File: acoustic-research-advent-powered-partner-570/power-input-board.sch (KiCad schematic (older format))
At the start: 13 parts, among them J24 DNP, SW1 MAIN POWER

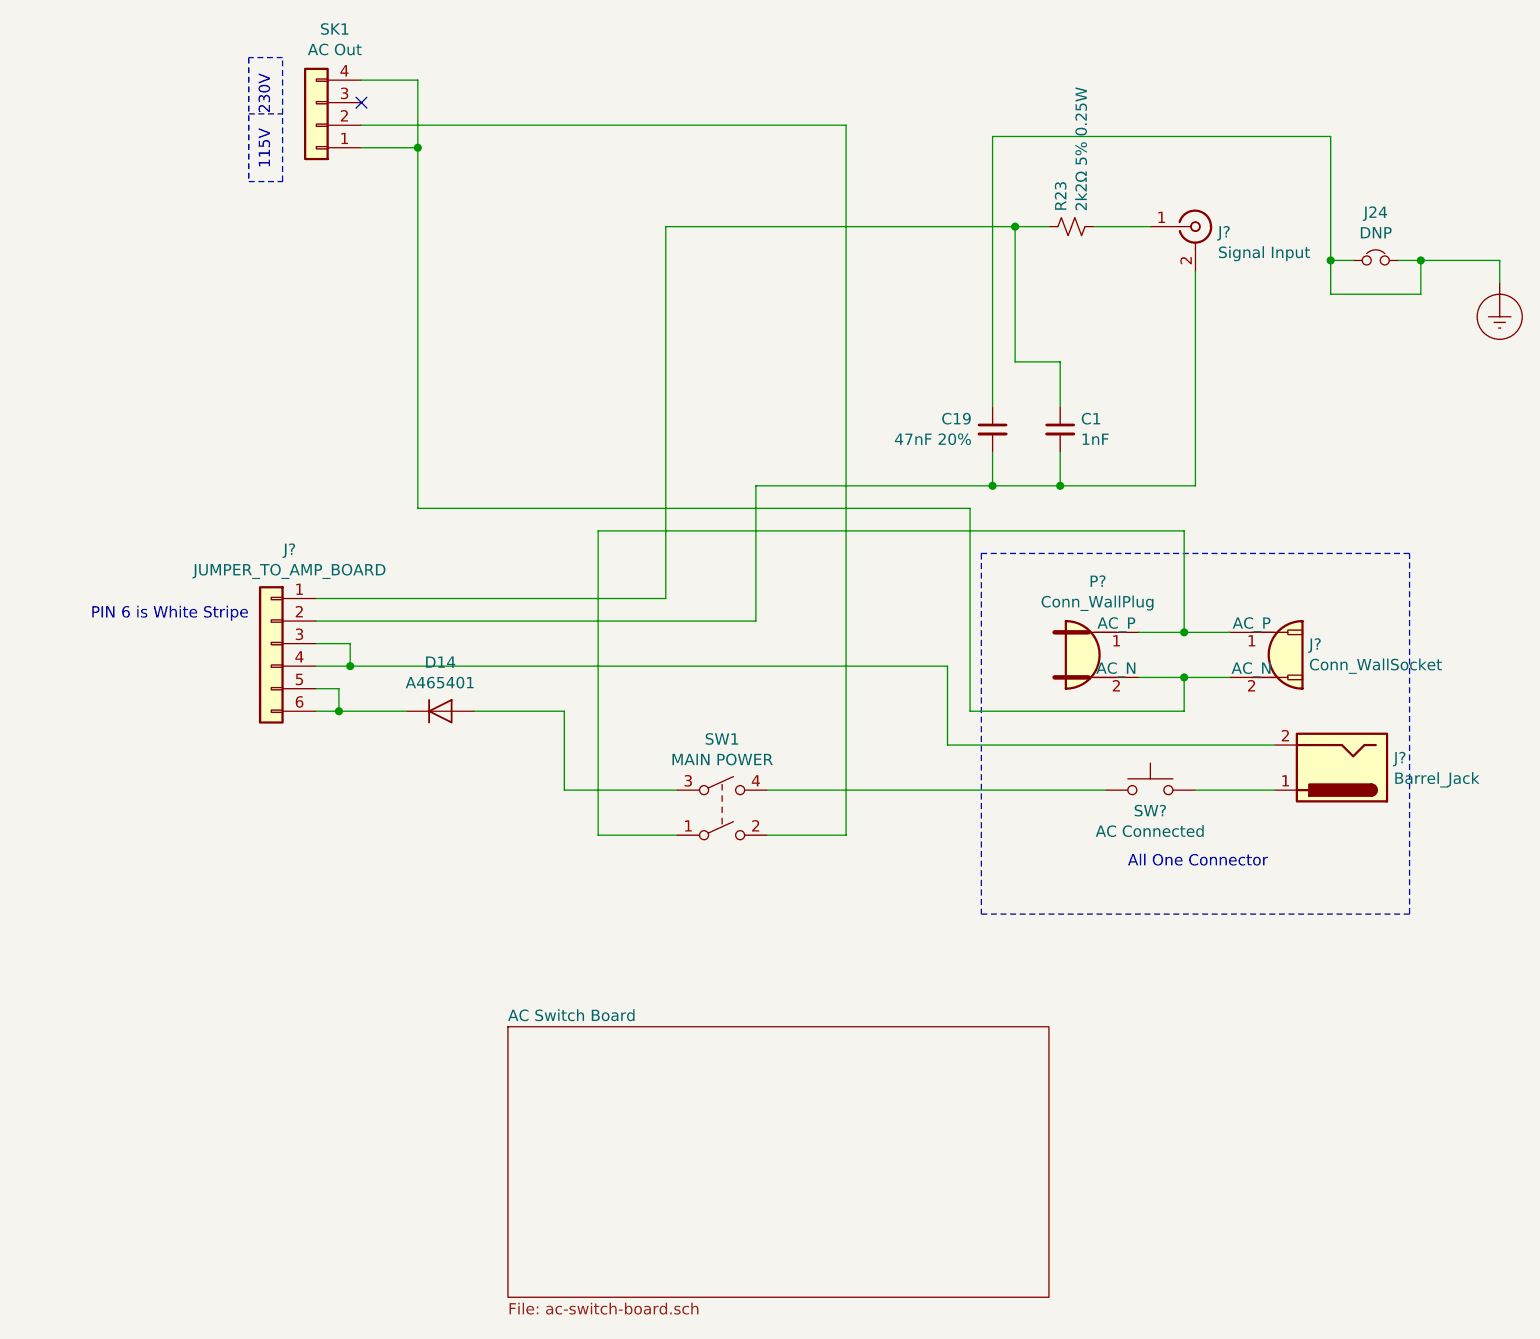
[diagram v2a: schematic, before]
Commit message: trying to clean schematic up a bit
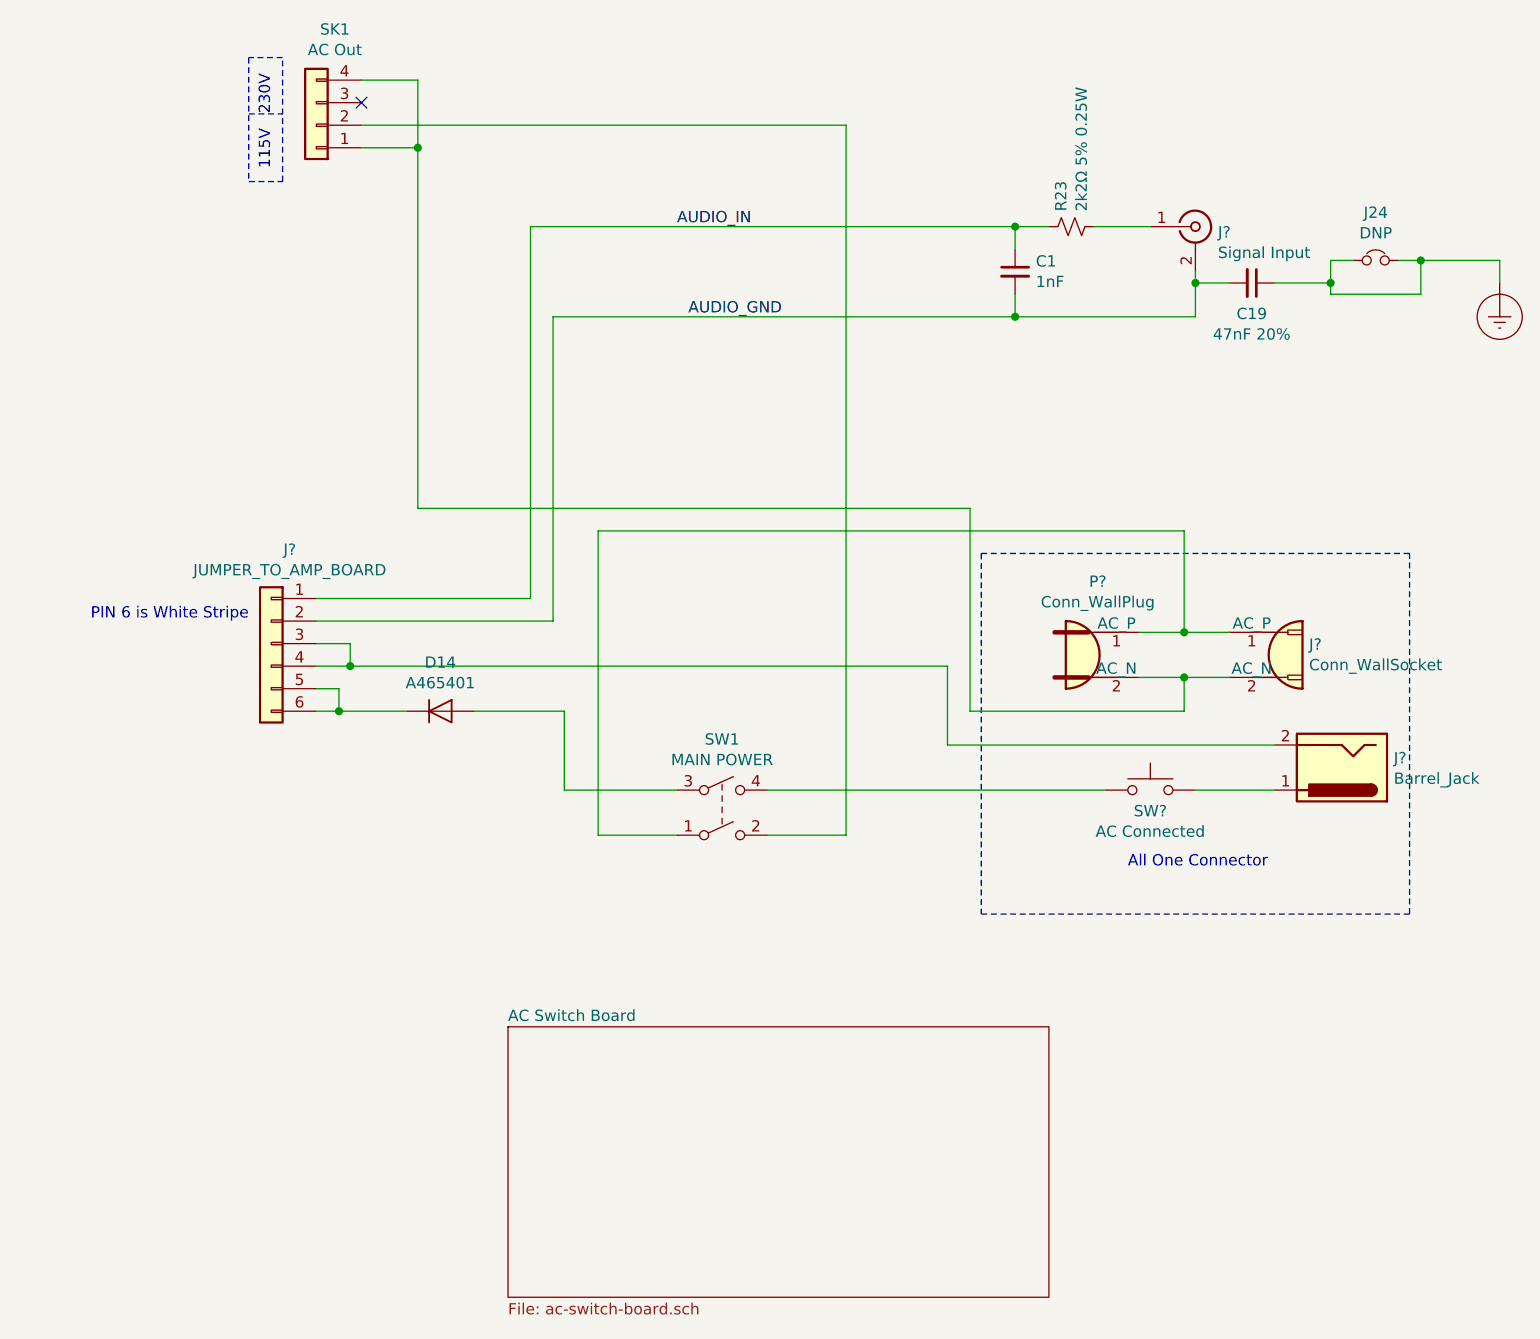
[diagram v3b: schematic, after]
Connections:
- net AUDIO_IN: now reaches C1.1, J?.1 (Pin_1), R23.1
- net AUDIO_GND: now reaches C1.2, C19.2, J?.2 (Ext), J?.2 (Pin_2)
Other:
- moved on the sheet: C1, C19
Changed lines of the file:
@@
 L Device:C_Small C19
 U 1 1 65811FCE
-P 5100 3250
-F 0 "C19" H 5008 3296 50  0000 R CNN
-F 1 "47nF 20%" H 5008 3205 50  0000 R CNN
-F 2 "" H 5100 3250 50  0001 C CNN
-F 3 "~" H 5100 3250 50  0001 C CNN
-	1    5100 3250
-	1    0    0    -1
+P 6250 2600
+F 0 "C19" V 6387 2600 50  0000 C CNN
+F 1 "47nF 20%" V 6478 2600 50  0000 C CNN
+F 2 "" H 6250 2600 50  0001 C CNN
+F 3 "~" H 6250 2600 50  0001 C CNN
+	1    6250 2600
+	0    1    1    0
 $EndComp
 $Comp
 L Device:C_Small C1
 U 1 1 65812993
-P 5400 3250
-F 0 "C1" H 5492 3296 50  0000 L CNN
-F 1 "1nF" H 5492 3205 50  0000 L CNN
-F 2 "" H 5400 3250 50  0001 C CNN
-F 3 "~" H 5400 3250 50  0001 C CNN
-	1    5400 3250
+P 5200 2550
+F 0 "C1" H 5292 2596 50  0000 L CNN
+F 1 "1nF" H 5292 2505 50  0000 L CNN
+F 2 "" H 5200 2550 50  0001 C CNN
+F 3 "~" H 5200 2550 50  0001 C CNN
+	1    5200 2550
 	1    0    0    -1
 $EndComp
@@
 $EndComp
 Wire Wire Line
-	6000 2550 6000 3500
-Wire Wire Line
-	6000 3500 5400 3500
-Wire Wire Line
-	4050 3500 4050 4100
-Wire Wire Line
-	4050 4100 2100 4100
-Wire Wire Line
-	5100 3350 5100 3500
-Connection ~ 5100 3500
-Wire Wire Line
-	5100 3500 4050 3500
-Wire Wire Line
-	5400 3350 5400 3500
-Connection ~ 5400 3500
-Wire Wire Line
-	5400 3500 5100 3500
+	6000 2550 6000 2600
+Wire Wire Line
+	6000 2750 5200 2750
+Wire Wire Line
+	3150 2750 3150 4100
+Wire Wire Line
+	3150 4100 2100 4100
+Connection ~ 5200 2750
 Wire Wire Line
 	7000 2500 7000 2650
@@
 	7000 2650 6600 2650
 Wire Wire Line
-	6600 2650 6600 2500
+	6600 2650 6600 2600
 Wire Wire Line
 	6600 2500 6700 2500
@@
 	7000 2500 7350 2500
 Wire Wire Line
-	5100 3150 5100 1950
-Wire Wire Line
-	5100 1950 6600 1950
-Wire Wire Line
-	6600 1950 6600 2500
-Connection ~ 6600 2500
-Wire Wire Line
 	5550 2350 5800 2350
 Wire Wire Line
-	5400 3150 5400 2950
-Wire Wire Line
-	5400 2950 5200 2950
-Wire Wire Line
-	5200 2950 5200 2350
-Wire Wire Line
 	5200 2350 5350 2350
 Wire Wire Line
-	5200 2350 3650 2350
-Wire Wire Line
-	3650 2350 3650 4000
-Wire Wire Line
-	3650 4000 2100 4000
+	5200 2350 3050 2350
+Wire Wire Line
+	3050 2350 3050 4000
+Wire Wire Line
+	3050 4000 2100 4000
 Connection ~ 5200 2350
 Wire Wire Line
@@
 Wire Wire Line
 	5600 4850 4100 4850
+Wire Wire Line
+	6150 2600 6000 2600
+Connection ~ 6000 2600
+Wire Wire Line
+	6000 2600 6000 2750
+Wire Wire Line
+	6350 2600 6600 2600
+Connection ~ 6600 2600
+Wire Wire Line
+	6600 2600 6600 2500
+Wire Wire Line
+	3150 2750 5200 2750
+Wire Wire Line
+	5200 2450 5200 2350
+Wire Wire Line
+	5200 2650 5200 2750
+Text Label 3700 2350 0    50   ~ 0
+AUDIO_IN
+Text Label 3750 2750 0    50   ~ 0
+AUDIO_GND
 $EndSCHEMATC
